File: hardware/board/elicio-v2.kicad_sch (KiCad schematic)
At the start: 66 parts, among them J1 TYPE-C-31-M-14, J2 SM02B-SRSS-TB, J3 HDR-3-RA, J4 TC2030-NL, P1 SIG1, P2 SIG2, P3 REF, Q1 AO3401A, Q2 2N7002, Q3 2N7002, Q4 2N7002, Q5 2N7002, SW1 4.5x4.5x1.6, U1 MDBT50Q-1MV2, U2 ADS1292IRSMT, U3 BQ25100YFPR, U4 TLV71330PDBVR, U5 USBLC6-2SC6

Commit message: fix(board-v2): take L7 quotes after page re-check
Co-authored-by: Cursor <cursoragent@cursor.com>
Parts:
- C2: LCSC C91601 -> C1524
- J2: LCSC C160404 -> C160402
- R11: LCSC C25848 -> C25917
- R12: LCSC C25841 -> C966759
- R13, R25, R26, R27, R28, R5, R6, R7, R8: LCSC C25792 -> C25744
- R17, R20, R21, R4: LCSC C2782127 -> C26083
- R18: LCSC C25780 -> C25792
- R29, R30: LCSC C25741 -> C26082
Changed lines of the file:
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@@
 			)
 		)
-		(property "LCSC" "C160404"
+		(property "LCSC" "C160402"
 			(at 25.4 165.1 0)
 			(show_name no)
@@
 			)
 		)
-		(property "LCSC" "C2782127"
+		(property "LCSC" "C26083"
 			(at 165.1 114.3 0)
 			(show_name no)
@@
 			)
 		)
-		(property "LCSC" "C25792"
+		(property "LCSC" "C25744"
 			(at 25.4 50.8 0)
 			(show_name no)
@@
 			)
 		)
-		(property "LCSC" "C25792"
+		(property "LCSC" "C25744"
 			(at 38.1 50.8 0)
 			(show_name no)
@@
 			)
 		)
-		(property "LCSC" "C25792"
+		(property "LCSC" "C25744"
 			(at 50.8 50.8 0)
 			(show_name no)
@@
 			)
 		)
-		(property "LCSC" "C25792"
+		(property "LCSC" "C25744"
 			(at 63.5 50.8 0)
 			(show_name no)
@@
 			)
 		)
-		(property "LCSC" "C25848"
+		(property "LCSC" "C25917"
 			(at 38.1 177.8 0)
 			(show_name no)
@@
 			)
 		)
-		(property "LCSC" "C25841"
+		(property "LCSC" "C966759"
 			(at 50.8 177.8 0)
 			(show_name no)
@@
 			)
 		)
-		(property "LCSC" "C25792"
+		(property "LCSC" "C25744"
 			(at 63.5 177.8 0)
 			(show_name no)
@@
 			)
 		)
-		(property "LCSC" "C91601"
+		(property "LCSC" "C1524"
 			(at 76.2 177.8 0)
 			(show_name no)
@@
 			)
 		)
-		(property "LCSC" "C2782127"
+		(property "LCSC" "C26083"
 			(at 139.7 127.0 0)
 			(show_name no)
@@
 			)
 		)
-		(property "LCSC" "C25780"
+		(property "LCSC" "C25792"
 			(at 76.2 50.8 0)
 			(show_name no)
@@
 			)
 		)
-		(property "LCSC" "C2782127"
+		(property "LCSC" "C26083"
 			(at 101.6 50.8 0)
 			(show_name no)
@@
 			)
 		)
-		(property "LCSC" "C2782127"
+		(property "LCSC" "C26083"
 			(at 114.3 50.8 0)
 			(show_name no)
@@
 			)
 		)
-		(property "LCSC" "C25792"
+		(property "LCSC" "C25744"
 			(at 152.4 50.8 0)
 			(show_name no)
@@
 			)
 		)
-		(property "LCSC" "C25792"
+		(property "LCSC" "C25744"
 			(at 25.4 25.4 0)
 			(show_name no)
@@
 			)
 		)
-		(property "LCSC" "C25792"
+		(property "LCSC" "C25744"
 			(at 165.1 38.1 0)
 			(show_name no)
@@
 			)
 		)
-		(property "LCSC" "C25792"
+		(property "LCSC" "C25744"
 			(at 177.8 38.1 0)
 			(show_name no)
@@
 			)
 		)
-		(property "LCSC" "C25741"
+		(property "LCSC" "C26082"
 			(at 177.8 127.0 0)
 			(show_name no)
@@
 			)
 		)
-		(property "LCSC" "C25741"
+		(property "LCSC" "C26082"
 			(at 190.5 127.0 0)
 			(show_name no)

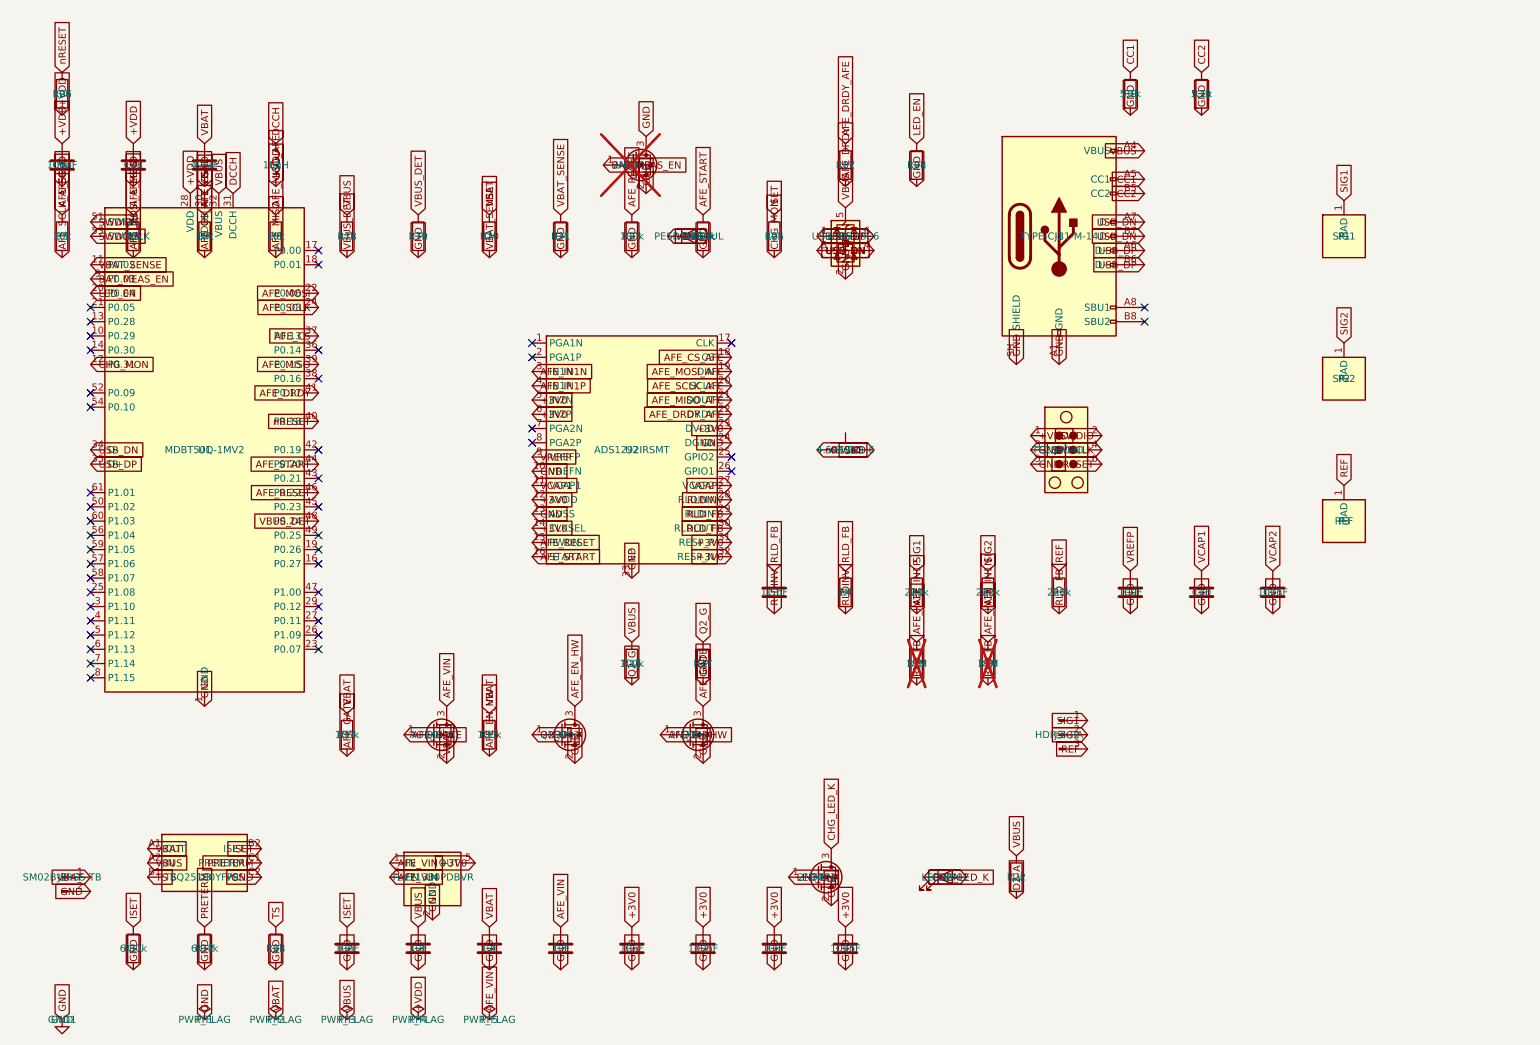
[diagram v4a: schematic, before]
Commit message: board(v2d): drop USB-C J1/U5; add tail charge pads P4/P5
Q81: VBUS comes from P4 through the existing P-FET and charger. D1 PESD stays on VBUS. nRF USB D+/D− are no-connect. ERC 0.
Co-authored-by: Cursor <cursoragent@cursor.com>
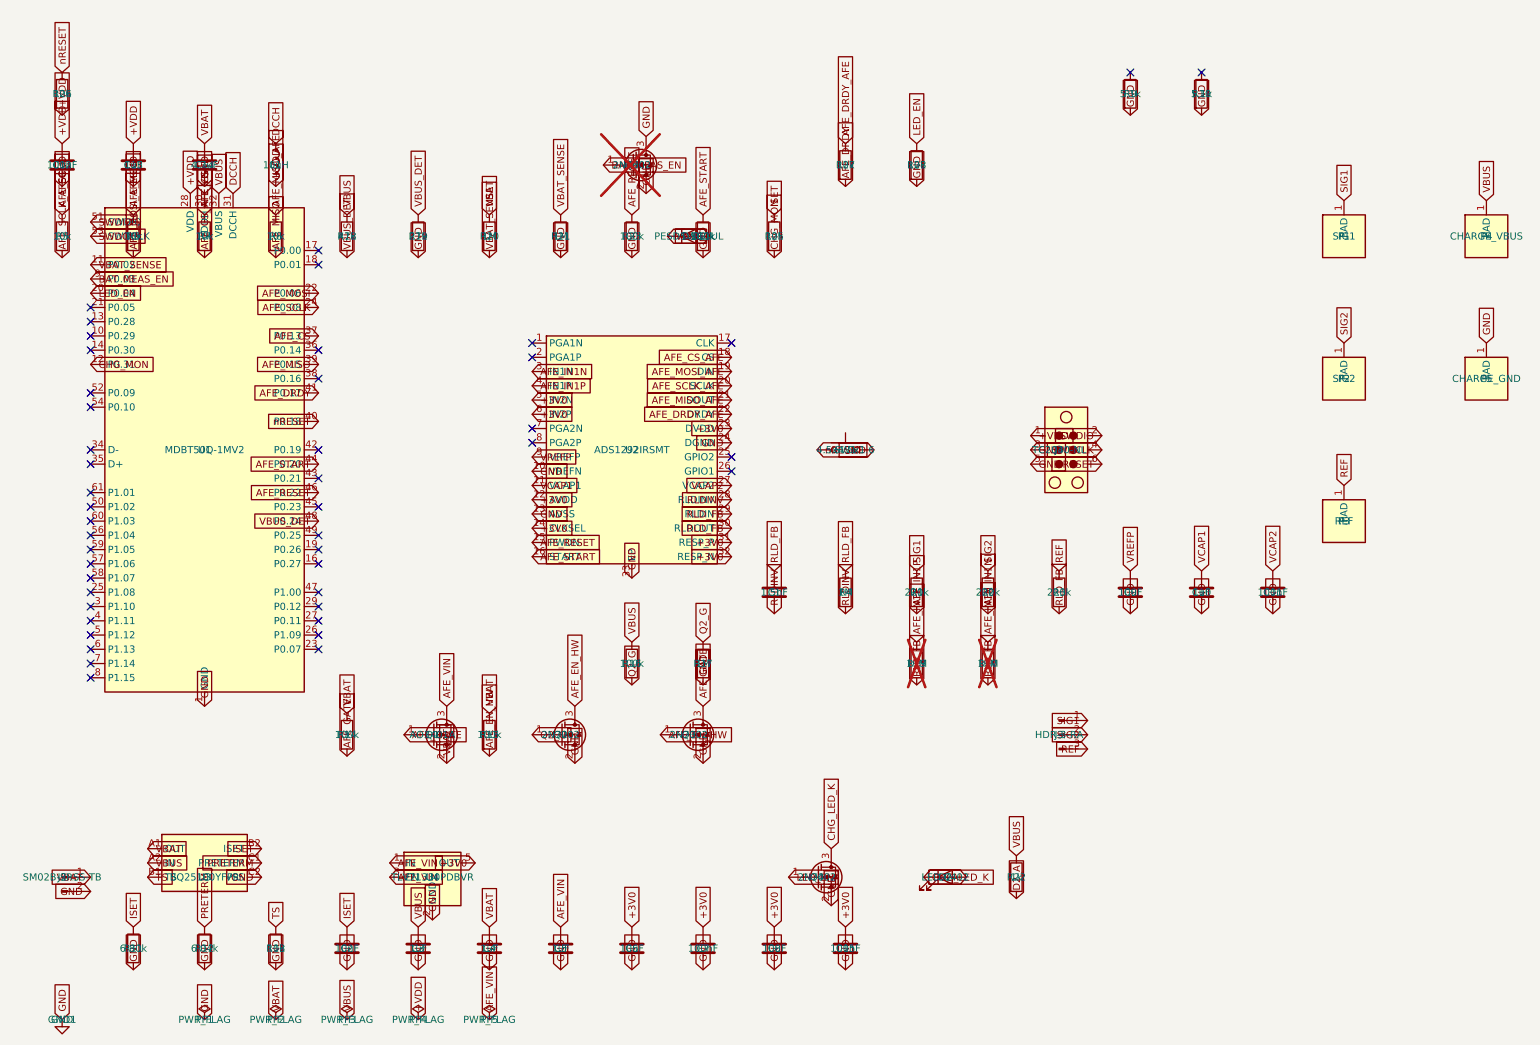
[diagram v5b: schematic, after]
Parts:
- removed J1: TYPE-C-31-M-14, Connector_USB:USB_C_Receptacle_HRO_TYPE-C-31-M-12, symbol Connector:USB_C_Receptacle_USB2.0_16P
- removed U5: USBLC6-2SC6, Package_TO_SOT_SMD:SOT-23-6, symbol elicio:USBLC6-2SC6
- added P4: CHARGE_VBUS, elicio:RING_PAD_D5_H2.7, symbol elicio:PAD_8x8
- added P5: CHARGE_GND, elicio:RING_PAD_D5_H2.7, symbol elicio:PAD_8x8
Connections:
- net GND: now also P5.1 (PAD)
- net VBUS: now also P4.1 (PAD)
- net CC1: no longer names the net of R9.1
- net CC2: no longer names the net of R10.1
- net USB_DN: no longer names the net of U1.34 (D-)
- net USB_DP: no longer names the net of U1.35 (D+)
- no-connect marks 44 -> 46

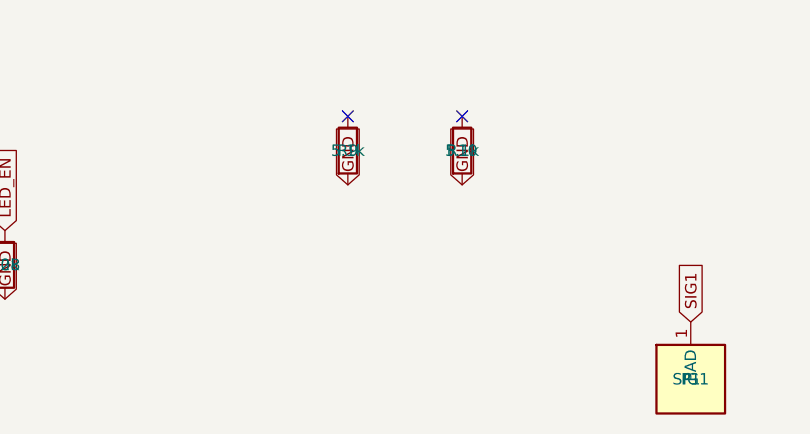
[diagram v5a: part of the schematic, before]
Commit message: board(v3): RSM land, R9/R10 DNP, Q94 stiffeners, Q97 tests; wait for pin table v3
U2 pads now match ADS1292 4219108/B (0.40 pitch, 0.55 x 0.20, EP 2.8). U3 stays YFP: the inner balls escape radially so there is no BOM swap. R9/R10 are DNP and off the PCB. Stiffeners sit only on a land-free face (count 9). The §5e parser is ready; it does not replace the vendored table until v3 lands.

Co-authored-by: Cursor <cursoragent@cursor.com>
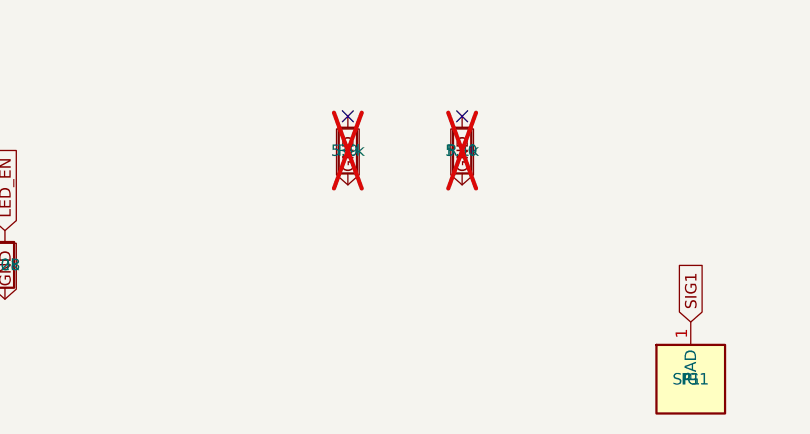
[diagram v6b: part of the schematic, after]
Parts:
- R10, R9: now not fitted; now left out of the parts list
- U2: footprint Package_DFN_QFN:VQFN-32-1EP_4x4mm_P0.4mm_EP2.8x2.8mm -> elicio:Texas_RSM0032
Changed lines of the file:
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@@
 		(date "2026-09-17")
 		(rev "0")
-		(comment 1 "WP12d board v2d. No USB-C receptacle (Q81). P4/P5 tail pads feed VBUS/GND. D1 PESD on VBUS. Not for order.")
+		(comment 1 "WP12i. U2 RSM land 4219108/B. U3 YFP kept. R9/R10 DNP (Q95). Not for order.")
 	)
 	(symbol
@@
 			)
 		)
-		(property "Footprint" "Package_DFN_QFN:VQFN-32-1EP_4x4mm_P0.4mm_EP2.8x2.8mm"
+		(property "Footprint" "elicio:Texas_RSM0032"
 			(at 127.0 88.9 0)
 			(show_name no)
@@
 		(body_style 1)
 		(exclude_from_sim no)
-		(in_bom yes)
-		(on_board yes)
-		(in_pos_files yes)
-		(dnp no)
+		(in_bom no)
+		(on_board no)
+		(in_pos_files no)
+		(dnp yes)
 		(property "Reference" "R9"
 			(at 215.9 25.4 0)
@@
 		(body_style 1)
 		(exclude_from_sim no)
-		(in_bom yes)
-		(on_board yes)
-		(in_pos_files yes)
-		(dnp no)
+		(in_bom no)
+		(on_board no)
+		(in_pos_files no)
+		(dnp yes)
 		(property "Reference" "R10"
 			(at 228.6 25.4 0)
